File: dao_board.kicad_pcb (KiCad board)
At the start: 2 copper layers, 80 x 57 mm, 44 parts, among them J1 DISH_LED, J10 KEY6, J11 KEY7, J12 START, J13 SELECT, J14 DISH_SENSOR, J3 SWD, J4 GPIO_EXPANSION, J5 KEY1, J6 KEY2, J7 KEY3, J8 KEY4, J9 KEY5, SW1 RESET, SW2 HX 3x4x2-2P-1.6N, U1 MDBT50Q-1MV2, U2 TLC6C598PWR, U3 TLC6C598PWR

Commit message: フォルダ整理なう、PCBデータのフットプリントの参照を変更前のコミット
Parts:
- D2: footprint Diode_SMD:D_SMA -> Library:D_SMA
- J3: footprint Connector:FanPinHeader_1x04_P2.54mm_Vertical -> Library:FanPinHeader_1x04_P2.54mm_Vertical
- J4: footprint Connector_PinHeader_2.54mm:PinHeader_2x05_P2.54mm_Vertical -> Library:PinHeader_2x05_P2.54mm_Vertical
- U1: footprint RF_Module:Raytac_MDBT50Q -> Library:Raytac_MDBT50Q
- U2, U3: footprint c2863406:TSSOP-16_L5.0-W4.4-P0.65-LS6.4-BL -> Library:TSSOP-16_L5.0-W4.4-P0.65-LS6.4-BL
- USBC1: footprint c165948:USB-C_SMD-TYPE-C-31-M-12_1 -> Library:USB-C_SMD-TYPE-C-31-M-12_1
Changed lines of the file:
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@@
 		(embedded_fonts no)
 	)
-	(footprint "c2863406:TSSOP-16_L5.0-W4.4-P0.65-LS6.4-BL"
+	(footprint "Library:TSSOP-16_L5.0-W4.4-P0.65-LS6.4-BL"
 		(layer "F.Cu")
 		(at 150.7861 127.0236 180)
@@
 			)
 		)
+		(property "LCSC" "C2863406"
+			(at 0 0 180)
+			(unlocked yes)
+			(layer "F.Fab")
+			(hide yes)
+			(effects
+				(font
+					(size 1 1)
+					(thickness 0.15)
+				)
+			)
+		)
 		(sheetname "/")
 		(sheetfile "dao_board.kicad_sch")
@@
 		)
 		(embedded_fonts no)
-		(model "c2863406.3dshapes/TSSOP-16_L5.0-W4.4-H1.0-LS6.4-P0.65.wrl"
+		(model "${KIPRJMOD}/footprints.pretty/TSSOP-16_L5.0-W4.4-H1.0-LS6.4-P0.65.step"
 			(offset
 				(xyz 0 0 0)
@@
 		)
 	)
-	(footprint "RF_Module:Raytac_MDBT50Q"
+	(footprint "Library:Raytac_MDBT50Q"
 		(layer "F.Cu")
 		(at 133.0361 108.196056)
@@
 		(embedded_fonts no)
 	)
-	(footprint "Diode_SMD:D_SMA"
+	(footprint "Library:D_SMA"
 		(layer "F.Cu")
 		(at 139.7861 135.8936)
@@
 		(embedded_fonts no)
 	)
-	(footprint "Connector:FanPinHeader_1x04_P2.54mm_Vertical"
+	(footprint "Library:FanPinHeader_1x04_P2.54mm_Vertical"
 		(layer "F.Cu")
 		(at 160.2861 109.4736 90)
@@
 		)
 	)
-	(footprint "c165948:USB-C_SMD-TYPE-C-31-M-12_1"
+	(footprint "Library:USB-C_SMD-TYPE-C-31-M-12_1"
 		(layer "F.Cu")
 		(at 148.7861 104.916056 180)
@@
 			)
 		)
+		(property "LCSC" "C165948"
+			(at 0 0 180)
+			(unlocked yes)
+			(layer "F.Fab")
+			(hide yes)
+			(effects
+				(font
+					(size 1 1)
+					(thickness 0.15)
+				)
+			)
+		)
 		(sheetname "/")
 		(sheetfile "dao_board.kicad_sch")
@@
 			)
 		)
+		(property "LCSC" "C49234124"
+			(at 0 0 90)
+			(unlocked yes)
+			(layer "F.Fab")
+			(hide yes)
+			(effects
+				(font
+					(size 1 1)
+					(thickness 0.15)
+				)
+			)
+		)
 		(sheetname "/")
 		(sheetfile "dao_board.kicad_sch")
@@
 			)
 		)
+		(property "LCSC" "C49234124"
+			(at 0 0 0)
+			(unlocked yes)
+			(layer "F.Fab")
+			(hide yes)
+			(effects
+				(font
+					(size 1 1)
+					(thickness 0.15)
+				)
+			)
+		)
 		(sheetname "/")
 		(sheetfile "dao_board.kicad_sch")
@@
 		)
 	)
-	(footprint "Connector_PinHeader_2.54mm:PinHeader_2x05_P2.54mm_Vertical"
+	(footprint "Library:PinHeader_2x05_P2.54mm_Vertical"
 		(layer "F.Cu")
 		(at 175.2461 122.8936)
@@
 		)
 	)
-	(footprint "c2863406:TSSOP-16_L5.0-W4.4-P0.65-LS6.4-BL"
+	(footprint "Library:TSSOP-16_L5.0-W4.4-P0.65-LS6.4-BL"
 		(layer "F.Cu")
 		(at 159.2861 126.8936)
@@
 			)
 		)
+		(property "LCSC" "C2863406"
+			(at 0 0 0)
+			(unlocked yes)
+			(layer "F.Fab")
+			(hide yes)
+			(effects
+				(font
+					(size 1 1)
+					(thickness 0.15)
+				)
+			)
+		)
 		(sheetname "/")
 		(sheetfile "dao_board.kicad_sch")
@@
 		)
 		(embedded_fonts no)
-		(model "c2863406.3dshapes/TSSOP-16_L5.0-W4.4-H1.0-LS6.4-P0.65.wrl"
+		(model "${KIPRJMOD}/footprints.pretty/TSSOP-16_L5.0-W4.4-H1.0-LS6.4-P0.65.step"
 			(offset
 				(xyz 0 0 0)

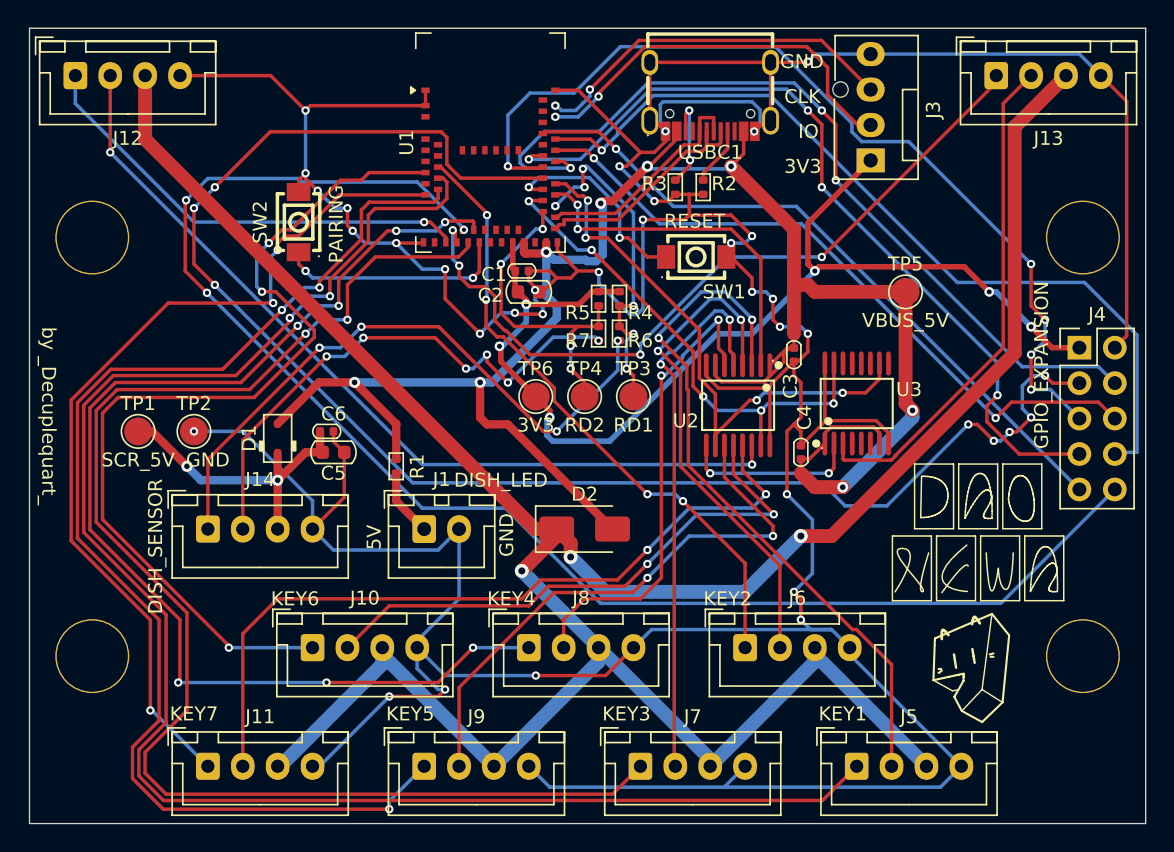
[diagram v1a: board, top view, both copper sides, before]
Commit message: 回路図から基板を更新、DRCの完全なクリアに成功
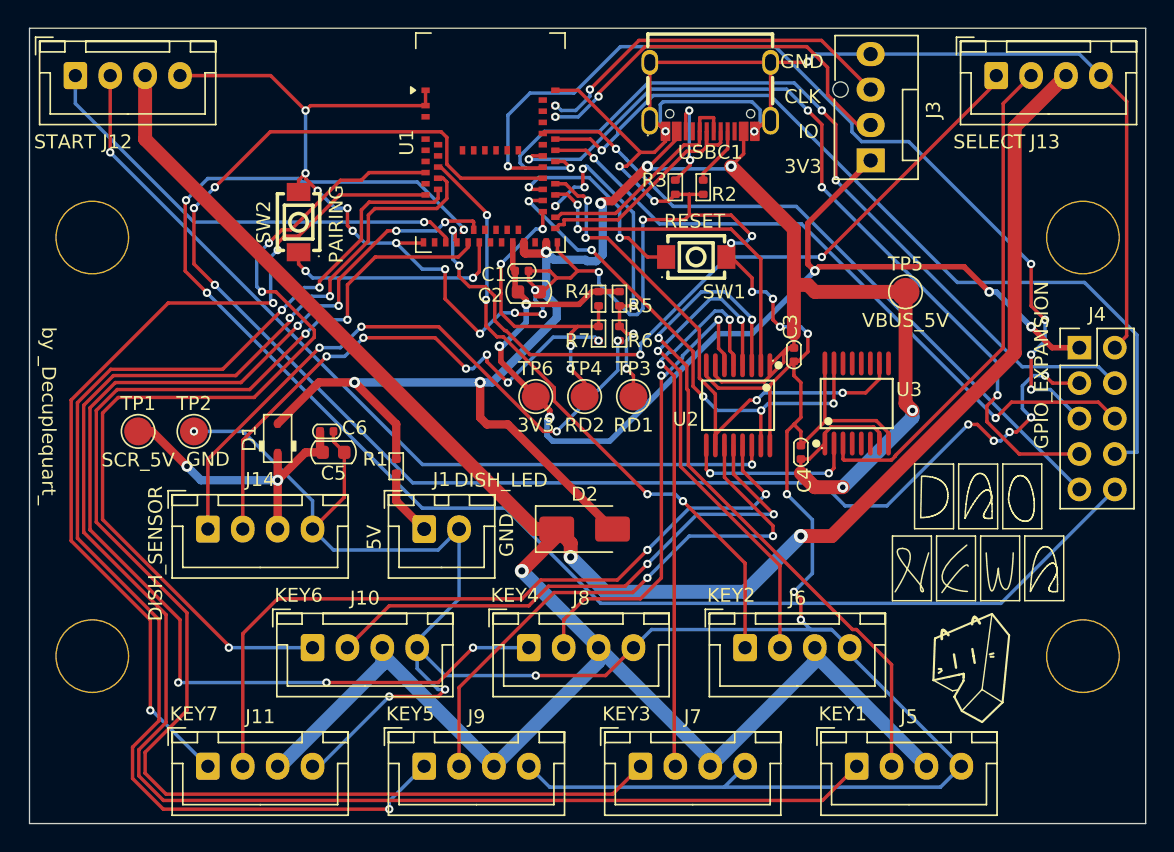
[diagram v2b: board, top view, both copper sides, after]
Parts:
- C1, C3, C4, C6: footprint Library:C_0402_1005Metric -> footprints:C_0402_1005Metric
- C2, C5: footprint Library:C_0603_1608Metric -> footprints:C_0603_1608Metric
- D1: footprint Library:D_SOD-323 -> footprints:D_SOD-323
- D2: footprint Library:D_SMA -> footprints:D_SMA
- H1, H2, H3, H4: footprint Library:MountingHole_M5 -> footprints:MountingHole_M5
- J1: footprint Library:JST_XH_B2B-XH-A_1x02_P2.50mm_Vertical -> footprints:JST_XH_B2B-XH-A_1x02_P2.50mm_Vertical
- J10, J11, J12, J13, J14, J5, J6, J7, J8, J9: footprint Library:JST_XH_B4B-XH-A_1x04_P2.50mm_Vertical -> footprints:JST_XH_B4B-XH-A_1x04_P2.50mm_Vertical
- J3: footprint Library:FanPinHeader_1x04_P2.54mm_Vertical -> footprints:FanPinHeader_1x04_P2.54mm_Vertical
- J4: footprint Library:PinHeader_2x05_P2.54mm_Vertical -> footprints:PinHeader_2x05_P2.54mm_Vertical
- R1, R2, R3, R4, R5, R6, R7: footprint Library:R_0402_1005Metric -> footprints:R_0402_1005Metric
- SW1, SW2: footprint Library:KEY-SMD_L4.0-W3.0-LS4.9-1 -> footprints:KEY-SMD_L4.0-W3.0-LS4.9-1
- TP1, TP2, TP3, TP4, TP5, TP6: footprint Library:TestPoint_Pad_D2.0mm -> footprints:TestPoint_Pad_D2.0mm
- U1: footprint Library:Raytac_MDBT50Q -> footprints:Raytac_MDBT50Q_FIXED
- U2, U3: footprint Library:TSSOP-16_L5.0-W4.4-P0.65-LS6.4-BL -> footprints:TSSOP-16_L5.0-W4.4-P0.65-LS6.4-BL
- USBC1: footprint Library:USB-C_SMD-TYPE-C-31-M-12_1 -> footprints:USB-C_SMD-TYPE-C-31-M-12_1_FIXED
